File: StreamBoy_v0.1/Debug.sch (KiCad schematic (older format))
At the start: 11 parts

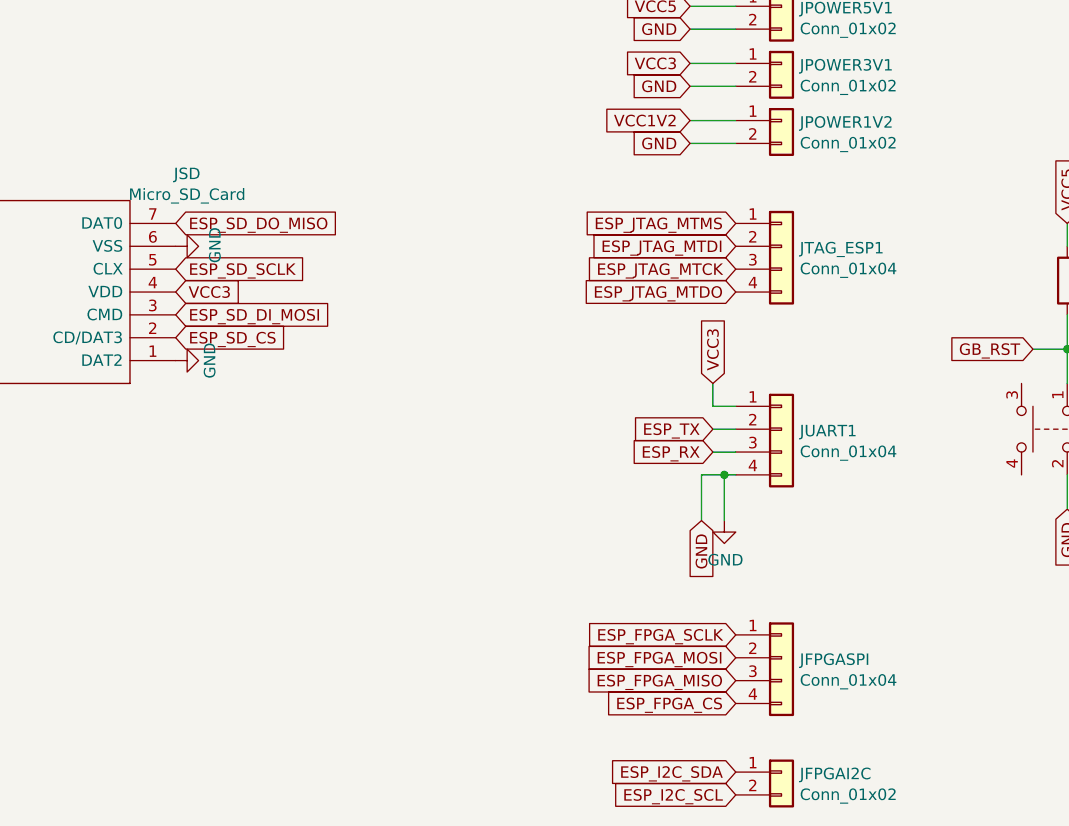
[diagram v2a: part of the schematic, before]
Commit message: Update some labels
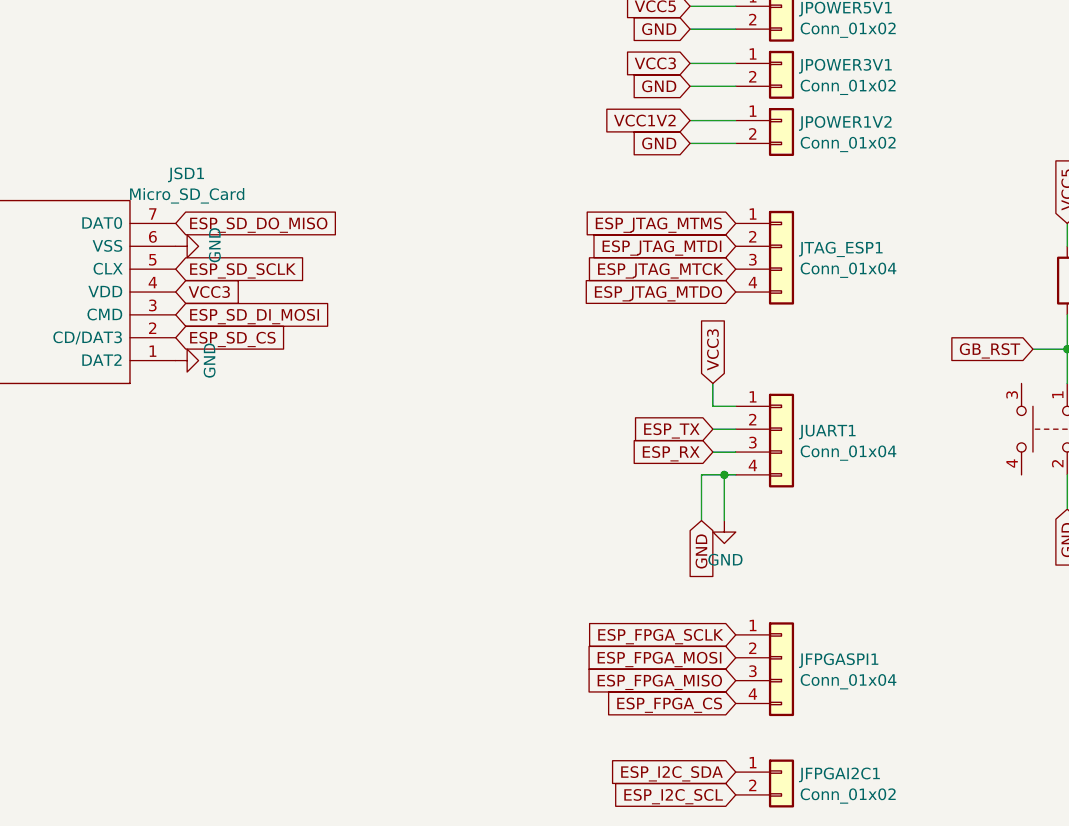
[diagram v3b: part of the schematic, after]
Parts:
- renumbered JFPGAI2C to JFPGAI2C1, JFPGASPI to JFPGASPI1, JSD to JSD1
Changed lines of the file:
@@
 P 7500 4800
 AR Path="/5E164B68" Ref="JTAG_ESP?"  Part="1"
-AR Path="/5E087685/5E164B68" Ref="JFPGASPI"  Part="1"
-F 0 "JFPGASPI" H 7580 4792 50  0000 L CNN
+AR Path="/5E087685/5E164B68" Ref="JFPGASPI1"  Part="1"
+F 0 "JFPGASPI1" H 7580 4792 50  0000 L CNN
 F 1 "Conn_01x04" H 7580 4701 50  0000 L CNN
 F 2 "Connector_PinHeader_2.54mm:PinHeader_1x04_P2.54mm_Vertical" H 7500 4800 50  0001 C CNN
@@
 P 7500 5300
 AR Path="/5E165AC9" Ref="JFPGA?"  Part="1"
-AR Path="/5E087685/5E165AC9" Ref="JFPGAI2C"  Part="1"
-F 0 "JFPGAI2C" H 7580 5292 50  0000 L CNN
+AR Path="/5E087685/5E165AC9" Ref="JFPGAI2C1"  Part="1"
+F 0 "JFPGAI2C1" H 7580 5292 50  0000 L CNN
 F 1 "Conn_01x02" H 7580 5201 50  0000 L CNN
 F 2 "Connector_PinHeader_2.54mm:PinHeader_1x02_P2.54mm_Vertical" H 7500 5300 50  0001 C CNN
@@
 	9250 3450 9050 3450
 $Comp
-L TF-015:TF-015 JSD
+L TF-015:TF-015 JSD1
 U 1 1 5E16DC93
 P 4850 3500
-F 0 "JSD" H 4800 2683 50  0000 C CNN
+F 0 "JSD1" H 4800 2683 50  0000 C CNN
 F 1 "Micro_SD_Card" H 4800 2774 50  0000 C CNN
 F 2 "TF-015:TF015" H 6000 3800 50  0001 C CNN
@@
 P 3550 3000
 AR Path="/5E17163C" Ref="#PWR?"  Part="1"
-AR Path="/5E087685/5E17163C" Ref="#PWR?"  Part="1"
-F 0 "#PWR?" H 3550 2750 50  0001 C CNN
+AR Path="/5E087685/5E17163C" Ref="#PWR0117"  Part="1"
+F 0 "#PWR0117" H 3550 2750 50  0001 C CNN
 F 1 "GND" H 3555 2827 50  0000 C CNN
 F 2 "" H 3550 3000 50  0001 C CNN
@@
 P 4850 3000
 AR Path="/5E173646" Ref="#PWR?"  Part="1"
-AR Path="/5E087685/5E173646" Ref="#PWR?"  Part="1"
-F 0 "#PWR?" H 4850 2750 50  0001 C CNN
+AR Path="/5E087685/5E173646" Ref="#PWR0118"  Part="1"
+F 0 "#PWR0118" H 4850 2750 50  0001 C CNN
 F 1 "GND" H 4855 2827 50  0000 C CNN
 F 2 "" H 4850 3000 50  0001 C CNN
@@
 P 4850 3500
 AR Path="/5E172C99" Ref="#PWR?"  Part="1"
-AR Path="/5E087685/5E172C99" Ref="#PWR?"  Part="1"
-F 0 "#PWR?" H 4850 3250 50  0001 C CNN
+AR Path="/5E087685/5E172C99" Ref="#PWR0119"  Part="1"
+F 0 "#PWR0119" H 4850 3250 50  0001 C CNN
 F 1 "GND" H 4850 3350 50  0000 C CNN
 F 2 "" H 4850 3500 50  0001 C CNN
@@
 P 3550 3100
 AR Path="/5E173024" Ref="#PWR?"  Part="1"
-AR Path="/5E087685/5E173024" Ref="#PWR?"  Part="1"
-F 0 "#PWR?" H 3550 2850 50  0001 C CNN
+AR Path="/5E087685/5E173024" Ref="#PWR0120"  Part="1"
+F 0 "#PWR0120" H 3550 2850 50  0001 C CNN
 F 1 "GND" H 3555 2927 50  0000 C CNN
 F 2 "" H 3550 3100 50  0001 C CNN
@@
 P 3550 3200
 AR Path="/5E096F86" Ref="#PWR?"  Part="1"
-AR Path="/5E087685/5E096F86" Ref="#PWR?"  Part="1"
-F 0 "#PWR?" H 3550 2950 50  0001 C CNN
+AR Path="/5E087685/5E096F86" Ref="#PWR0121"  Part="1"
+F 0 "#PWR0121" H 3550 2950 50  0001 C CNN
 F 1 "GND" H 3555 3027 50  0000 C CNN
 F 2 "" H 3550 3200 50  0001 C CNN
@@
 P 3550 3300
 AR Path="/5E097212" Ref="#PWR?"  Part="1"
-AR Path="/5E087685/5E097212" Ref="#PWR?"  Part="1"
-F 0 "#PWR?" H 3550 3050 50  0001 C CNN
+AR Path="/5E087685/5E097212" Ref="#PWR0122"  Part="1"
+F 0 "#PWR0122" H 3550 3050 50  0001 C CNN
 F 1 "GND" H 3555 3127 50  0000 C CNN
 F 2 "" H 3550 3300 50  0001 C CNN
@@
 P 3550 3500
 AR Path="/5E097405" Ref="#PWR?"  Part="1"
-AR Path="/5E087685/5E097405" Ref="#PWR?"  Part="1"
-F 0 "#PWR?" H 3550 3250 50  0001 C CNN
+AR Path="/5E087685/5E097405" Ref="#PWR0123"  Part="1"
+F 0 "#PWR0123" H 3550 3250 50  0001 C CNN
 F 1 "GND" H 3555 3327 50  0000 C CNN
 F 2 "" H 3550 3500 50  0001 C CNN
@@
 P 3550 3400
 AR Path="/5E097DDA" Ref="#PWR?"  Part="1"
-AR Path="/5E087685/5E097DDA" Ref="#PWR?"  Part="1"
-F 0 "#PWR?" H 3550 3150 50  0001 C CNN
+AR Path="/5E087685/5E097DDA" Ref="#PWR0124"  Part="1"
+F 0 "#PWR0124" H 3550 3150 50  0001 C CNN
 F 1 "GND" H 3555 3227 50  0000 C CNN
 F 2 "" H 3550 3400 50  0001 C CNN

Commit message: Add leds and buttons to debug
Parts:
- added D? (x4): LED, LED_SMD:LED_1210_3225Metric, symbol Device:LED
- added R? (x6): 4.7K, Resistor_SMD:R_0805_2012Metric, symbol Device:R
- added SW_B1, SW_B2: SW_Push, Button_Switch_THT:SW_PUSH_6mm, symbol Switch:SW_Push
- SW_RESET_GB1: symbol Switch:SW_Push_Dual -> Switch:SW_Push
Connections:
- net labels added: ESP_BUTTON1, ESP_BUTTON2, ESP_LED1, ESP_LED2, FPGA_LED1, FPGA_LED2
- wire segments 22 -> 45
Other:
- moved on the sheet: JDAC1, JFPGAI2C1, JFPGASPI1, JPOWER1V2, JPOWER3V1, JPOWER5V1, JSD1, JTAG_ESP1, JUART1, R42

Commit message: More renumbering
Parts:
- JUART1: value Conn_01x04 -> Conn_01x06; footprint Connector_PinHeader_2.54mm:PinHeader_1x04_P2.54mm_Vertical -> Connector_PinHeader_2.54mm:PinHeader_1x06_P2.54mm_Vertical; symbol Connector_Generic:Conn_01x04 -> Connector_Generic:Conn_01x06
- gave numbers to parts that had none: 10
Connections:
- net labels added: ESP_DTR, ESP_RTS
- wire segments 45 -> 47
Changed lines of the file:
@@
 	7200 1850 7400 1850
 $Comp
-L Connector_Generic:Conn_01x04 JUART?
+L Connector_Generic:Conn_01x06 JUART?
 U 1 1 5E0943DC
 P 7600 3350
@@
 AR Path="/5E087685/5E0943DC" Ref="JUART1"  Part="1"
 F 0 "JUART1" H 7680 3342 50  0000 L CNN
-F 1 "Conn_01x04" H 7680 3251 50  0000 L CNN
-F 2 "Connector_PinHeader_2.54mm:PinHeader_1x04_P2.54mm_Vertical" H 7600 3350 50  0001 C CNN
+F 1 "Conn_01x06" H 7680 3251 50  0000 L CNN
+F 2 "Connector_PinHeader_2.54mm:PinHeader_1x06_P2.54mm_Vertical" H 7600 3350 50  0001 C CNN
 F 3 "~" H 7600 3350 50  0001 C CNN
 	1    7600 3350
 	1    0    0    -1
 $EndComp
-Text GLabel 7300 3250 0    50   Input ~ 0
+Text GLabel 7300 3150 0    50   Input ~ 0
 VCC3
-Text GLabel 7300 3550 0    50   Input ~ 0
+Text GLabel 7300 3650 0    50   Input ~ 0
 GND
 $Comp
 L power:GND #PWR?
 U 1 1 5E0943E4
-P 7400 3650
+P 7400 3750
 AR Path="/5E0943E4" Ref="#PWR?"  Part="1"
 AR Path="/5E087685/5E0943E4" Ref="#PWR0104"  Part="1"
-F 0 "#PWR0104" H 7400 3400 50  0001 C CNN
-F 1 "GND" H 7405 3477 50  0000 C CNN
-F 2 "" H 7400 3650 50  0001 C CNN
-F 3 "" H 7400 3650 50  0001 C CNN
-	1    7400 3650
+F 0 "#PWR0104" H 7400 3500 50  0001 C CNN
+F 1 "GND" H 7405 3577 50  0000 C CNN
+F 2 "" H 7400 3750 50  0001 C CNN
+F 3 "" H 7400 3750 50  0001 C CNN
+	1    7400 3750
 	1    0    0    -1
 $EndComp
@@
 	1    0    0    -1
 $EndComp
-Text GLabel 7300 3450 0    50   Input ~ 0
+Text GLabel 7300 3350 0    50   Input ~ 0
 ESP_RX
-Text GLabel 7300 3350 0    50   Input ~ 0
+Text GLabel 7300 3250 0    50   Input ~ 0
 ESP_TX
 Wire Wire Line
-	7400 3450 7300 3450
-Wire Wire Line
-	7300 3350 7400 3350
-Connection ~ 7400 3550
-Wire Wire Line
-	7400 3550 7300 3550
-Wire Wire Line
-	7400 3250 7300 3250
+	7400 3350 7300 3350
+Wire Wire Line
+	7300 3250 7400 3250
+Wire Wire Line
+	7400 3650 7300 3650
+Wire Wire Line
+	7400 3150 7300 3150
 $Comp
 L Device:R R?
@@
 P 2600 5850
 AR Path="/5E1A6938" Ref="#PWR?"  Part="1"
-AR Path="/5E087685/5E1A6938" Ref="#PWR?"  Part="1"
-F 0 "#PWR?" H 2600 5600 50  0001 C CNN
+AR Path="/5E087685/5E1A6938" Ref="#PWR0117"  Part="1"
+F 0 "#PWR0117" H 2600 5600 50  0001 C CNN
 F 1 "GND" H 2605 5677 50  0000 C CNN
 F 2 "" H 2600 5850 50  0001 C CNN
@@
 P 2600 5300
 AR Path="/5E1A7067" Ref="#PWR?"  Part="1"
-AR Path="/5E087685/5E1A7067" Ref="#PWR?"  Part="1"
-F 0 "#PWR?" H 2600 5050 50  0001 C CNN
+AR Path="/5E087685/5E1A7067" Ref="#PWR0120"  Part="1"
+F 0 "#PWR0120" H 2600 5050 50  0001 C CNN
 F 1 "GND" H 2605 5127 50  0000 C CNN
 F 2 "" H 2600 5300 50  0001 C CNN
@@
 P 1800 5300
 AR Path="/5E1A71D2" Ref="R?"  Part="1"
-AR Path="/5E087685/5E1A71D2" Ref="R?"  Part="1"
-F 0 "R?" H 1730 5254 50  0000 R CNN
+AR Path="/5E087685/5E1A71D2" Ref="R13"  Part="1"
+F 0 "R13" H 1730 5254 50  0000 R CNN
 F 1 "4.7K" H 1730 5345 50  0000 R CNN
 F 2 "Resistor_SMD:R_0805_2012Metric" V 1730 5300 50  0001 C CNN
@@
 P 1800 5850
 AR Path="/5E1A778B" Ref="R?"  Part="1"
-AR Path="/5E087685/5E1A778B" Ref="R?"  Part="1"
-F 0 "R?" H 1730 5804 50  0000 R CNN
+AR Path="/5E087685/5E1A778B" Ref="R14"  Part="1"
+F 0 "R14" H 1730 5804 50  0000 R CNN
 F 1 "4.7K" H 1730 5895 50  0000 R CNN
 F 2 "Resistor_SMD:R_0805_2012Metric" V 1730 5850 50  0001 C CNN
@@
 P 1900 3950
 AR Path="/5E1A91FA" Ref="R?"  Part="1"
-AR Path="/5E087685/5E1A91FA" Ref="R?"  Part="1"
-F 0 "R?" H 1830 3904 50  0000 R CNN
+AR Path="/5E087685/5E1A91FA" Ref="R19"  Part="1"
+F 0 "R19" H 1830 3904 50  0000 R CNN
 F 1 "4.7K" H 1830 3995 50  0000 R CNN
 F 2 "Resistor_SMD:R_0805_2012Metric" V 1830 3950 50  0001 C CNN
@@
 P 1900 3150
 AR Path="/5E1A9DCF" Ref="R?"  Part="1"
-AR Path="/5E087685/5E1A9DCF" Ref="R?"  Part="1"
-F 0 "R?" H 1830 3104 50  0000 R CNN
+AR Path="/5E087685/5E1A9DCF" Ref="R18"  Part="1"
+F 0 "R18" H 1830 3104 50  0000 R CNN
 F 1 "4.7K" H 1830 3195 50  0000 R CNN
 F 2 "Resistor_SMD:R_0805_2012Metric" V 1830 3150 50  0001 C CNN
@@
 P 2200 3950
 AR Path="/5E1ABE75" Ref="#PWR?"  Part="1"
-AR Path="/5E087685/5E1ABE75" Ref="#PWR?"  Part="1"
-F 0 "#PWR?" H 2200 3700 50  0001 C CNN
+AR Path="/5E087685/5E1ABE75" Ref="#PWR0121"  Part="1"
+F 0 "#PWR0121" H 2200 3700 50  0001 C CNN
 F 1 "GND" H 2205 3777 50  0000 C CNN
 F 2 "" H 2200 3950 50  0001 C CNN
@@
 P 2200 3150
 AR Path="/5E1AC0F0" Ref="#PWR?"  Part="1"
-AR Path="/5E087685/5E1AC0F0" Ref="#PWR?"  Part="1"
-F 0 "#PWR?" H 2200 2900 50  0001 C CNN
+AR Path="/5E087685/5E1AC0F0" Ref="#PWR0122"  Part="1"
+F 0 "#PWR0122" H 2200 2900 50  0001 C CNN
 F 1 "GND" H 2205 2977 50  0000 C CNN
 F 2 "" H 2200 3150 50  0001 C CNN
@@
 	2250 3800 2150 3800
 $Comp
-L Device:LED D?
+L Device:LED D3
 U 1 1 5E1ADE0C
 P 2250 5300
-F 0 "D?" H 2243 5045 50  0000 C CNN
+F 0 "D3" H 2243 5045 50  0000 C CNN
 F 1 "LED" H 2243 5136 50  0000 C CNN
 F 2 "LED_SMD:LED_1210_3225Metric" H 2250 5300 50  0001 C CNN
@@
 $EndComp
 $Comp
-L Device:LED D?
+L Device:LED D4
 U 1 1 5E1AE59E
 P 2250 5850
-F 0 "D?" H 2243 5595 50  0000 C CNN
+F 0 "D4" H 2243 5595 50  0000 C CNN
 F 1 "LED" H 2243 5686 50  0000 C CNN
 F 2 "LED_SMD:LED_1210_3225Metric" H 2250 5850 50  0001 C CNN
@@
 P 2600 6400
 AR Path="/5E1BF25C" Ref="#PWR?"  Part="1"
-AR Path="/5E087685/5E1BF25C" Ref="#PWR?"  Part="1"
-F 0 "#PWR?" H 2600 6150 50  0001 C CNN
+AR Path="/5E087685/5E1BF25C" Ref="#PWR0124"  Part="1"
+F 0 "#PWR0124" H 2600 6150 50  0001 C CNN
 F 1 "GND" H 2605 6227 50  0000 C CNN
 F 2 "" H 2600 6400 50  0001 C CNN
@@
 P 1800 6400
 AR Path="/5E1BF262" Ref="R?"  Part="1"
-AR Path="/5E087685/5E1BF262" Ref="R?"  Part="1"
-F 0 "R?" H 1730 6354 50  0000 R CNN
+AR Path="/5E087685/5E1BF262" Ref="R15"  Part="1"
+F 0 "R15" H 1730 6354 50  0000 R CNN
 F 1 "4.7K" H 1730 6445 50  0000 R CNN
 F 2 "Resistor_SMD:R_0805_2012Metric" V 1730 6400 50  0001 C CNN
@@
 	1650 6400 1450 6400
 $Comp
-L Device:LED D?
+L Device:LED D5
 U 1 1 5E1BF269
 P 2250 6400
-F 0 "D?" H 2243 6145 50  0000 C CNN
+F 0 "D5" H 2243 6145 50  0000 C CNN
 F 1 "LED" H 2243 6236 50  0000 C CNN
 F 2 "LED_SMD:LED_1210_3225Metric" H 2250 6400 50  0001 C CNN
@@
 P 2600 6900
 AR Path="/5E1C0AC9" Ref="#PWR?"  Part="1"
-AR Path="/5E087685/5E1C0AC9" Ref="#PWR?"  Part="1"
-F 0 "#PWR?" H 2600 6650 50  0001 C CNN
+AR Path="/5E087685/5E1C0AC9" Ref="#PWR0131"  Part="1"
+F 0 "#PWR0131" H 2600 6650 50  0001 C CNN
 F 1 "GND" H 2605 6727 50  0000 C CNN
 F 2 "" H 2600 6900 50  0001 C CNN
@@
 P 1800 6900
 AR Path="/5E1C0ACF" Ref="R?"  Part="1"
-AR Path="/5E087685/5E1C0ACF" Ref="R?"  Part="1"
-F 0 "R?" H 1730 6854 50  0000 R CNN
+AR Path="/5E087685/5E1C0ACF" Ref="R17"  Part="1"
+F 0 "R17" H 1730 6854 50  0000 R CNN
 F 1 "4.7K" H 1730 6945 50  0000 R CNN
 F 2 "Resistor_SMD:R_0805_2012Metric" V 1730 6900 50  0001 C CNN
@@
 	1650 6900 1450 6900
 $Comp
-L Device:LED D?
+L Device:LED D6
 U 1 1 5E1C0AD6
 P 2250 6900
-F 0 "D?" H 2243 6645 50  0000 C CNN
+F 0 "D6" H 2243 6645 50  0000 C CNN
 F 1 "LED" H 2243 6736 50  0000 C CNN
 F 2 "LED_SMD:LED_1210_3225Metric" H 2250 6900 50  0001 C CNN
@@
 	2400 6900 2600 6900
 Wire Wire Line
-	7400 3550 7400 3650
-Wire Wire Line
 	1150 1900 1150 1700
 Connection ~ 1150 1300
@@
 Wire Wire Line
 	1150 1700 1150 1600
+Wire Wire Line
+	7400 3750 7400 3650
+Connection ~ 7400 3650
+Text GLabel 7300 3450 0    50   Input ~ 0
+ESP_DTR
+Text GLabel 7300 3550 0    50   Input ~ 0
+ESP_RTS
+Wire Wire Line
+	7400 3450 7300 3450
+Wire Wire Line
+	7300 3550 7400 3550
 $EndSCHEMATC

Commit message: Replace reset button with a jumper
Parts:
- removed SW_RESET_GB1: SW_Push, Button_Switch_THT:SW_PUSH_6mm, symbol Switch:SW_Push
- added JRESET: Conn_01x02, Connector_PinHeader_2.54mm:PinHeader_1x02_P2.54mm_Vertical, symbol Connector_Generic:Conn_01x02
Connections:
- net labels added: GB_VIN
- wire segments 47 -> 50
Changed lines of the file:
@@
 	-1   0    0    1
 $EndComp
-$Comp
-L Switch:SW_Push SW_RESET_GB?
-U 1 1 5E094405
-P 4300 3350
-AR Path="/5E094405" Ref="SW_RESET_GB?"  Part="1"
-AR Path="/5E087685/5E094405" Ref="SW_RESET_GB1"  Part="1"
-F 0 "SW_RESET_GB1" V 4254 3498 50  0000 L CNN
-F 1 "SW_Push" V 4345 3498 50  0000 L CNN
-F 2 "Button_Switch_THT:SW_PUSH_6mm" H 4300 3550 50  0001 C CNN
-F 3 "" H 4300 3550 50  0001 C CNN
-	1    4300 3350
-	0    -1   1    0
-$EndComp
-Text GLabel 4300 3700 3    50   Input ~ 0
+Text GLabel 4300 3400 3    50   Input ~ 0
 GND
 Text GLabel 4300 2450 1    50   Input ~ 0
@@
 	4300 2850 4300 3000
 Wire Wire Line
-	4300 3550 4300 3700
+	4300 3250 4300 3400
 Wire Wire Line
 	4300 3000 4100 3000
@@
 	7250 1150 7400 1150
 Wire Wire Line
-	7400 1050 7250 1050
+	7400 1050 7350 1050
 Text GLabel 5450 3000 2    50   Input ~ 0
 ESP_GB_RESET
@@
 Wire Wire Line
 	7300 3550 7400 3550
+Text GLabel 7250 950  0    50   Input ~ 0
+GB_VIN
+Wire Wire Line
+	7250 950  7350 950
+Wire Wire Line
+	7350 950  7350 1050
+Connection ~ 7350 1050
+Wire Wire Line
+	7350 1050 7250 1050
+$Comp
+L Connector_Generic:Conn_01x02 JPOWER1V?
+U 1 1 5E28641F
+P 4500 3150
+AR Path="/5E28641F" Ref="JPOWER1V?"  Part="1"
+AR Path="/5E087685/5E28641F" Ref="JRESET"  Part="1"
+F 0 "JRESET" H 4580 3142 50  0000 L CNN
+F 1 "Conn_01x02" H 4580 3051 50  0000 L CNN
+F 2 "Connector_PinHeader_2.54mm:PinHeader_1x02_P2.54mm_Vertical" H 4500 3150 50  0001 C CNN
+F 3 "~" H 4500 3150 50  0001 C CNN
+	1    4500 3150
+	1    0    0    -1
+$EndComp
 $EndSCHEMATC

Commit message: I hate component placement!
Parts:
- R13, R14, R15, R17, R18, R19: value 4.7K -> 4.7KOhm; footprint Resistor_SMD:R_0805_2012Metric -> Resistor_SMD:R_0402_1005Metric; lcscPartnum (none) -> C25900
- renumbered JRESET to JRESET1
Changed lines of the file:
@@
 EESchema Schematic File Version 4
-LIBS:StreamBoy-cache
-EELAYER 29 0
+EELAYER 30 0
 EELAYER END
 $Descr A4 11693 8268
@@
 AR Path="/5E087685/5E1A71D2" Ref="R13"  Part="1"
 F 0 "R13" H 1730 5254 50  0000 R CNN
-F 1 "4.7K" H 1730 5345 50  0000 R CNN
-F 2 "Resistor_SMD:R_0805_2012Metric" V 1730 5300 50  0001 C CNN
+F 1 "4.7KOhm" H 1730 5345 50  0000 R CNN
+F 2 "Resistor_SMD:R_0402_1005Metric" V 1730 5300 50  0001 C CNN
 F 3 "~" H 1800 5300 50  0001 C CNN
+F 4 "C25900" H 1800 5300 50  0001 C CNN "lcscPartnum"
 	1    1800 5300
 	0    -1   -1   0
@@
 AR Path="/5E087685/5E1A778B" Ref="R14"  Part="1"
 F 0 "R14" H 1730 5804 50  0000 R CNN
-F 1 "4.7K" H 1730 5895 50  0000 R CNN
-F 2 "Resistor_SMD:R_0805_2012Metric" V 1730 5850 50  0001 C CNN
+F 1 "4.7KOhm" H 1730 5895 50  0000 R CNN
+F 2 "Resistor_SMD:R_0402_1005Metric" V 1730 5850 50  0001 C CNN
 F 3 "~" H 1800 5850 50  0001 C CNN
+F 4 "C25900" H 1800 5850 50  0001 C CNN "lcscPartnum"
 	1    1800 5850
 	0    -1   -1   0
@@
 AR Path="/5E087685/5E1A91FA" Ref="R19"  Part="1"
 F 0 "R19" H 1830 3904 50  0000 R CNN
-F 1 "4.7K" H 1830 3995 50  0000 R CNN
-F 2 "Resistor_SMD:R_0805_2012Metric" V 1830 3950 50  0001 C CNN
+F 1 "4.7KOhm" H 1830 3995 50  0000 R CNN
+F 2 "Resistor_SMD:R_0402_1005Metric" V 1830 3950 50  0001 C CNN
 F 3 "~" H 1900 3950 50  0001 C CNN
+F 4 "C25900" H 1900 3950 50  0001 C CNN "lcscPartnum"
 	1    1900 3950
 	0    1    1    0
@@
 AR Path="/5E087685/5E1A9DCF" Ref="R18"  Part="1"
 F 0 "R18" H 1830 3104 50  0000 R CNN
-F 1 "4.7K" H 1830 3195 50  0000 R CNN
-F 2 "Resistor_SMD:R_0805_2012Metric" V 1830 3150 50  0001 C CNN
+F 1 "4.7KOhm" H 1830 3195 50  0000 R CNN
+F 2 "Resistor_SMD:R_0402_1005Metric" V 1830 3150 50  0001 C CNN
 F 3 "~" H 1900 3150 50  0001 C CNN
+F 4 "C25900" H 1900 3150 50  0001 C CNN "lcscPartnum"
 	1    1900 3150
 	0    1    1    0
@@
 AR Path="/5E087685/5E1BF262" Ref="R15"  Part="1"
 F 0 "R15" H 1730 6354 50  0000 R CNN
-F 1 "4.7K" H 1730 6445 50  0000 R CNN
-F 2 "Resistor_SMD:R_0805_2012Metric" V 1730 6400 50  0001 C CNN
+F 1 "4.7KOhm" H 1730 6445 50  0000 R CNN
+F 2 "Resistor_SMD:R_0402_1005Metric" V 1730 6400 50  0001 C CNN
 F 3 "~" H 1800 6400 50  0001 C CNN
+F 4 "C25900" H 1800 6400 50  0001 C CNN "lcscPartnum"
 	1    1800 6400
 	0    -1   -1   0
@@
 AR Path="/5E087685/5E1C0ACF" Ref="R17"  Part="1"
 F 0 "R17" H 1730 6854 50  0000 R CNN
-F 1 "4.7K" H 1730 6945 50  0000 R CNN
-F 2 "Resistor_SMD:R_0805_2012Metric" V 1730 6900 50  0001 C CNN
+F 1 "4.7KOhm" H 1730 6945 50  0000 R CNN
+F 2 "Resistor_SMD:R_0402_1005Metric" V 1730 6900 50  0001 C CNN
 F 3 "~" H 1800 6900 50  0001 C CNN
+F 4 "C25900" H 1800 6900 50  0001 C CNN "lcscPartnum"
 	1    1800 6900
 	0    -1   -1   0
@@
 P 4500 3150
 AR Path="/5E28641F" Ref="JPOWER1V?"  Part="1"
-AR Path="/5E087685/5E28641F" Ref="JRESET"  Part="1"
-F 0 "JRESET" H 4580 3142 50  0000 L CNN
+AR Path="/5E087685/5E28641F" Ref="JRESET1"  Part="1"
+F 0 "JRESET1" H 4580 3142 50  0000 L CNN
 F 1 "Conn_01x02" H 4580 3051 50  0000 L CNN
 F 2 "Connector_PinHeader_2.54mm:PinHeader_1x02_P2.54mm_Vertical" H 4500 3150 50  0001 C CNN
